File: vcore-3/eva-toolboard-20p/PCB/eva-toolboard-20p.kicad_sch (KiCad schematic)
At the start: 10 parts, among them J1 TH0, J2 HEATER, J3 STEPPER, J4 Main connector, J5 HOTENDFAN, J6 PARTFAN_1, J7 PARTFAN_2, J8 ENDSTOP_X, J9 PROBE

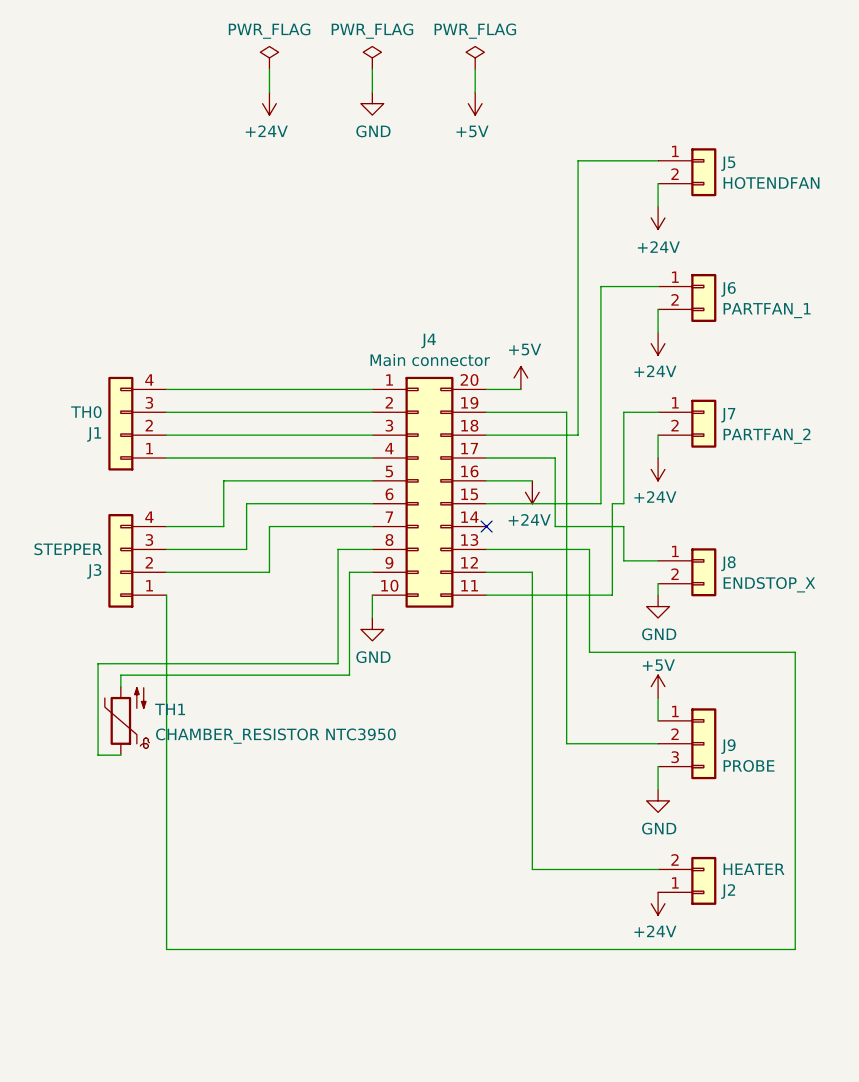
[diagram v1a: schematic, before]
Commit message: Added Neopixel and unified part fan V-
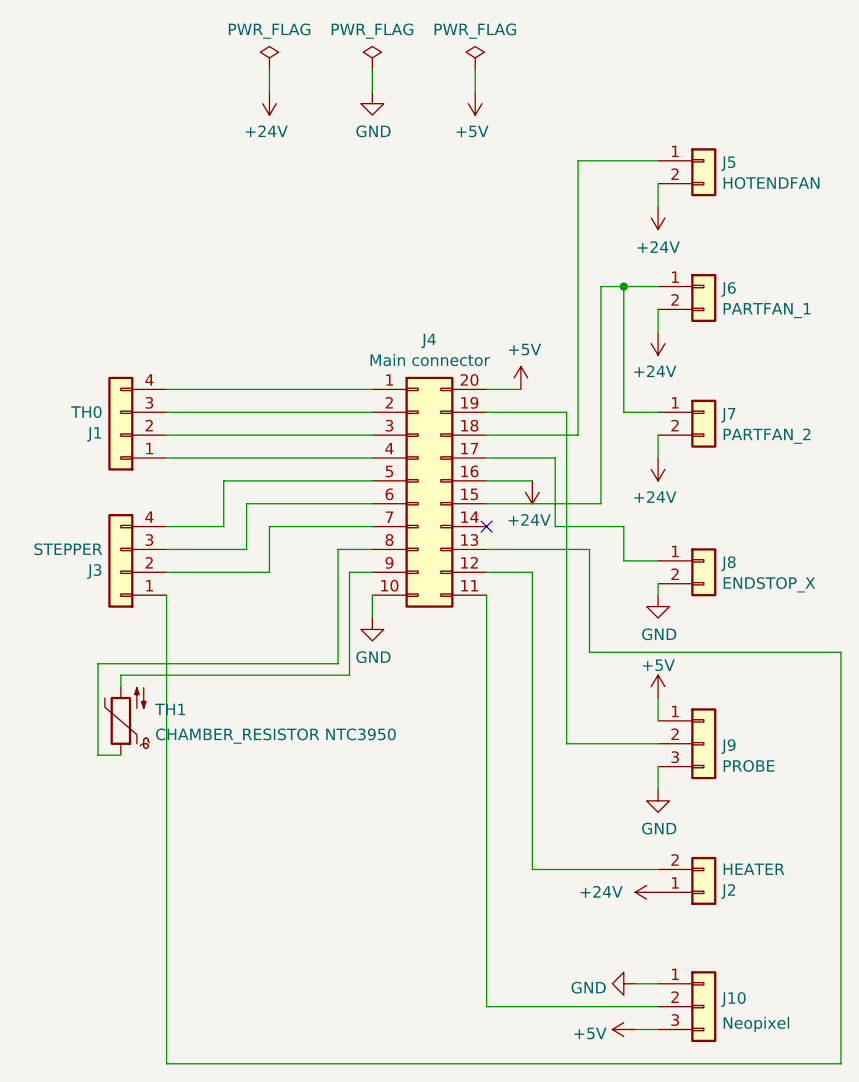
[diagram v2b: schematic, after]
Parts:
- added J10: Neopixel, Connector_JST:JST_PH_S3B-PH-K_1x03_P2.00mm_Horizontal, symbol Connector_Generic:Conn_01x03
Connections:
- net +5V: now also J10.3 (Pin_3)
- net GND: now also J10.1 (Pin_1)
- net at J4.11 (Pin_11): now also J10.2 (Pin_2); no longer J7.1 (Pin_1)
- net at J4.15 (Pin_15), J6.1 (Pin_1): now also J7.1 (Pin_1)
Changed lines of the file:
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@@
 (kicad_sch (version 20211123) (generator eeschema)
   (paper "A4")
+  (junction (at 162.56 63.5) (diameter 0) (color 0 0 0 0)
+  )
   (no_connect (at 147.32 90.17))
   (wire (pts (xy 111.76 80.01) (xy 134.62 80.01))
@@
     (stroke (width 0) (type default) (color 0 0 0 0))
   )
-  (wire (pts (xy 161.29 87.63) (xy 161.29 97.79))
-    (stroke (width 0) (type default) (color 0 0 0 0))
-  )
   (wire (pts (xy 156.21 114.3) (xy 166.37 114.3))
     (stroke (width 0) (type default) (color 0 0 0 0))
@@
     (stroke (width 0) (type default) (color 0 0 0 0))
   )
-  (wire (pts (xy 181.61 137.16) (xy 181.61 104.14))
-    (stroke (width 0) (type default) (color 0 0 0 0))
-  )
   (wire (pts (xy 111.76 82.55) (xy 134.62 82.55))
     (stroke (width 0) (type default) (color 0 0 0 0))
@@
     (stroke (width 0) (type default) (color 0 0 0 0))
   )
-  (wire (pts (xy 166.37 63.5) (xy 160.02 63.5))
+  (wire (pts (xy 163.83 146.05) (xy 166.37 146.05))
+    (stroke (width 0) (type default) (color 0 0 0 0))
+  )
+  (wire (pts (xy 186.69 149.86) (xy 111.76 149.86))
+    (stroke (width 0) (type default) (color 0 0 0 0))
+  )
+  (wire (pts (xy 166.37 63.5) (xy 162.56 63.5))
     (stroke (width 0) (type default) (color 0 0 0 0))
   )
@@
     (stroke (width 0) (type default) (color 0 0 0 0))
   )
+  (wire (pts (xy 163.83 140.97) (xy 166.37 140.97))
+    (stroke (width 0) (type default) (color 0 0 0 0))
+  )
   (wire (pts (xy 152.4 95.25) (xy 152.4 128.27))
     (stroke (width 0) (type default) (color 0 0 0 0))
@@
     (stroke (width 0) (type default) (color 0 0 0 0))
   )
+  (wire (pts (xy 186.69 104.14) (xy 186.69 149.86))
+    (stroke (width 0) (type default) (color 0 0 0 0))
+  )
+  (wire (pts (xy 162.56 63.5) (xy 160.02 63.5))
+    (stroke (width 0) (type default) (color 0 0 0 0))
+  )
   (wire (pts (xy 134.62 41.91) (xy 134.62 39.37))
     (stroke (width 0) (type default) (color 0 0 0 0))
   )
-  (wire (pts (xy 161.29 97.79) (xy 147.32 97.79))
-    (stroke (width 0) (type default) (color 0 0 0 0))
-  )
   (wire (pts (xy 134.62 92.71) (xy 130.81 92.71))
     (stroke (width 0) (type default) (color 0 0 0 0))
@@
     (stroke (width 0) (type default) (color 0 0 0 0))
   )
-  (wire (pts (xy 111.76 137.16) (xy 181.61 137.16))
-    (stroke (width 0) (type default) (color 0 0 0 0))
-  )
-  (wire (pts (xy 181.61 104.14) (xy 158.75 104.14))
+  (wire (pts (xy 158.75 104.14) (xy 186.69 104.14))
     (stroke (width 0) (type default) (color 0 0 0 0))
   )
@@
     (stroke (width 0) (type default) (color 0 0 0 0))
   )
-  (wire (pts (xy 111.76 97.79) (xy 111.76 137.16))
+  (wire (pts (xy 111.76 97.79) (xy 111.76 149.86))
     (stroke (width 0) (type default) (color 0 0 0 0))
   )
@@
     (stroke (width 0) (type default) (color 0 0 0 0))
   )
-  (wire (pts (xy 162.56 77.47) (xy 162.56 87.63))
-    (stroke (width 0) (type default) (color 0 0 0 0))
-  )
   (wire (pts (xy 118.11 85.09) (xy 134.62 85.09))
     (stroke (width 0) (type default) (color 0 0 0 0))
@@
     (stroke (width 0) (type default) (color 0 0 0 0))
   )
+  (wire (pts (xy 162.56 63.5) (xy 162.56 77.47))
+    (stroke (width 0) (type default) (color 0 0 0 0))
+  )
   (wire (pts (xy 166.37 109.22) (xy 166.37 111.76))
     (stroke (width 0) (type default) (color 0 0 0 0))
@@
     (stroke (width 0) (type default) (color 0 0 0 0))
   )
+  (wire (pts (xy 166.37 143.51) (xy 147.32 143.51))
+    (stroke (width 0) (type default) (color 0 0 0 0))
+  )
   (wire (pts (xy 154.94 90.17) (xy 154.94 82.55))
     (stroke (width 0) (type default) (color 0 0 0 0))
@@
     (stroke (width 0) (type default) (color 0 0 0 0))
   )
+  (wire (pts (xy 147.32 143.51) (xy 147.32 97.79))
+    (stroke (width 0) (type default) (color 0 0 0 0))
+  )
   (wire (pts (xy 166.37 68.58) (xy 166.37 66.04))
     (stroke (width 0) (type default) (color 0 0 0 0))
@@
   )
   (wire (pts (xy 123.19 95.25) (xy 123.19 90.17))
-    (stroke (width 0) (type default) (color 0 0 0 0))
-  )
-  (wire (pts (xy 162.56 87.63) (xy 161.29 87.63))
     (stroke (width 0) (type default) (color 0 0 0 0))
   )
@@
     (pin "1")
   )
-  (symbol (lib_id "power:+24V") (at 166.37 130.81 180) (unit 1)
-    (in_bom yes) (on_board yes)
-    (property "Reference" "#PWR0105" (id 0) (at 166.37 127 0)
-      (effects (font (size 1.27 1.27)) hide)
-    )
-    (property "Value" "+24V" (id 1) (at 165.989 135.2042 0))
+  (symbol (lib_id "power:+24V") (at 166.37 130.81 90) (unit 1)
+    (in_bom yes) (on_board yes)
+    (property "Reference" "#PWR0105" (id 0) (at 170.18 130.81 0)
+      (effects (font (size 1.27 1.27)) hide)
+    )
+    (property "Value" "+24V" (id 1) (at 160.02 130.81 90))
     (property "Footprint" "" (id 2) (at 166.37 130.81 0)
       (effects (font (size 1.27 1.27)) hide)
@@
     )
     (pin "1")
+  )
+  (symbol (lib_id "power:GND") (at 163.83 140.97 270) (unit 1)
+    (in_bom yes) (on_board yes) (fields_autoplaced)
+    (property "Reference" "#PWR0108" (id 0) (at 157.48 140.97 0)
+      (effects (font (size 1.27 1.27)) hide)
+    )
+    (property "Value" "GND" (id 1) (at 160.6551 141.449 90)
+      (effects (font (size 1.27 1.27)) (justify right))
+    )
+    (property "Footprint" "" (id 2) (at 163.83 140.97 0)
+      (effects (font (size 1.27 1.27)) hide)
+    )
+    (property "Datasheet" "" (id 3) (at 163.83 140.97 0)
+      (effects (font (size 1.27 1.27)) hide)
+    )
+    (pin "1")
+  )
+  (symbol (lib_id "Connector_Generic:Conn_01x03") (at 171.45 143.51 0) (unit 1)
+    (in_bom yes) (on_board yes) (fields_autoplaced)
+    (property "Reference" "J10" (id 0) (at 173.482 142.6015 0)
+      (effects (font (size 1.27 1.27)) (justify left))
+    )
+    (property "Value" "Neopixel" (id 1) (at 173.482 145.3766 0)
+      (effects (font (size 1.27 1.27)) (justify left))
+    )
+    (property "Footprint" "Connector_JST:JST_PH_S3B-PH-K_1x03_P2.00mm_Horizontal" (id 2) (at 171.45 143.51 0)
+      (effects (font (size 1.27 1.27)) hide)
+    )
+    (property "Datasheet" "~" (id 3) (at 171.45 143.51 0)
+      (effects (font (size 1.27 1.27)) hide)
+    )
+    (pin "1")
+    (pin "2")
+    (pin "3")
   )
   (symbol (lib_id "power:+24V") (at 166.37 54.61 180) (unit 1)
@@
     (pin "2")
   )
+  (symbol (lib_id "power:+5V") (at 163.83 146.05 90) (unit 1)
+    (in_bom yes) (on_board yes) (fields_autoplaced)
+    (property "Reference" "#PWR0107" (id 0) (at 167.64 146.05 0)
+      (effects (font (size 1.27 1.27)) hide)
+    )
+    (property "Value" "+5V" (id 1) (at 160.6551 146.529 90)
+      (effects (font (size 1.27 1.27)) (justify left))
+    )
+    (property "Footprint" "" (id 2) (at 163.83 146.05 0)
+      (effects (font (size 1.27 1.27)) hide)
+    )
+    (property "Datasheet" "" (id 3) (at 163.83 146.05 0)
+      (effects (font (size 1.27 1.27)) hide)
+    )
+    (pin "1")
+  )
   (sheet_instances
     (path "/" (page "1"))
@@
       (reference "#PWR0106") (unit 1) (value "+24V") (footprint "")
     )
+    (path "/ff233927-4d6d-4aaa-992e-0b8cab2147c0"
+      (reference "#PWR0107") (unit 1) (value "+5V") (footprint "")
+    )
+    (path "/32b16043-bf77-4ef3-a0eb-e36b415725f2"
+      (reference "#PWR0108") (unit 1) (value "GND") (footprint "")
+    )
     (path "/00000000-0000-0000-0000-000061bf6f32"
       (reference "J1") (unit 1) (value "TH0") (footprint "Connector_JST:JST_PH_B4B-PH-K_1x04_P2.00mm_Vertical")
@@
       (reference "J9") (unit 1) (value "PROBE") (footprint "Connector_JST:JST_PH_S3B-PH-K_1x03_P2.00mm_Horizontal")
     )
+    (path "/b6e4df8e-850d-44e1-8d92-bece851f1dfa"
+      (reference "J10") (unit 1) (value "Neopixel") (footprint "Connector_JST:JST_PH_S3B-PH-K_1x03_P2.00mm_Horizontal")
+    )
     (path "/d75c37f0-192f-4dd7-8bb8-fca15c330491"
